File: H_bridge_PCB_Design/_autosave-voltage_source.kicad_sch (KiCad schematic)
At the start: 27 parts, among them IC1 LM2671M-3.3_NOPB, IC2 L7812ABD2T-TR, J15 TSW-102-15-T-S, U6 LD1086DT50TR, U8 3544-2

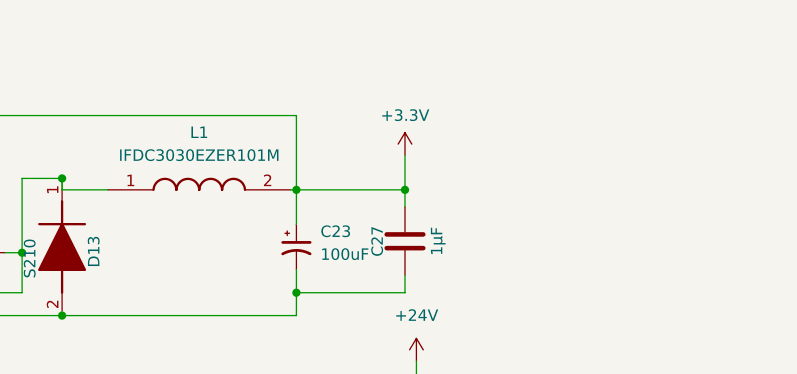
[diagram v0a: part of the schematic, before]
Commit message: -Changed PCB Layout now with 2x 3.3V also from usb, and to different ground planes -Measurement output now correctly parametrized -Stop sequence changed for SC protection
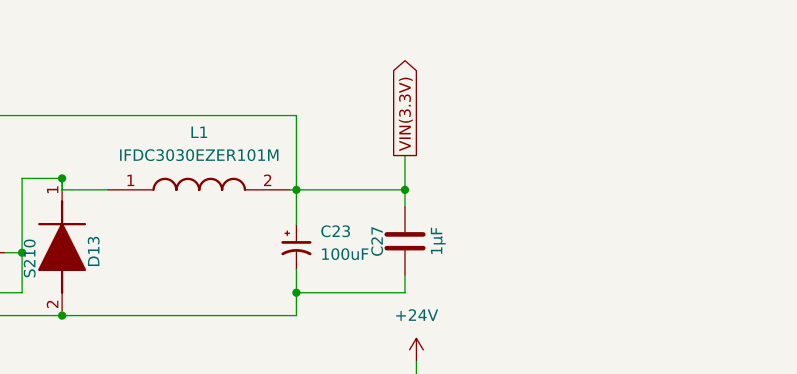
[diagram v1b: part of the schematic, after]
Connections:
- net +3.3V: no longer C23.1, C27.1, IC1.4 (FB), L1.2
- new net VIN(3.3V): C23.1, C27.1, IC1.4 (FB), L1.2
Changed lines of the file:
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@@
+		)
+	)
+	(global_label "VIN(3.3V)"
+		(shape output)
+		(at 220.98 35.56 90)
+		(fields_autoplaced yes)
+		(effects
+			(font
+				(size 1.27 1.27)
+			)
+			(justify left)
+		)
+		(property "Intersheetrefs" "${INTERSHEET_REFS}"
+			(at 220.98 23.7451 90)
+			(effects
+				(font
+					(size 1.27 1.27)
+				)
+				(justify left)
+				(hide yes)
+			)
 		)
 	)
@@
 			)
 		)
-	)
-	(symbol
-		(lib_id "power:+3.3V")
-		(at 220.98 35.56 0)
-		(unit 1)
-		(exclude_from_sim no)
-		(in_bom yes)
-		(on_board yes)
-		(dnp no)
-		(fields_autoplaced yes)
-		(property "Reference" "#PWR035"
-			(at 220.98 39.37 0)
-			(effects
-				(font
-					(size 1.27 1.27)
-				)
-				(hide yes)
-			)
-		)
-		(property "Value" "+3.3V"
-			(at 220.98 31.115 0)
-			(effects
-				(font
-					(size 1.27 1.27)
-				)
-			)
-		)
-		(property "Footprint" ""
-			(at 220.98 35.56 0)
-			(effects
-				(font
-					(size 1.27 1.27)
-				)
-				(hide yes)
-			)
-		)
-		(property "Datasheet" ""
-			(at 220.98 35.56 0)
-			(effects
-				(font
-					(size 1.27 1.27)
-				)
-				(hide yes)
-			)
-		)
-		(property "Description" "Power symbol creates a global label with name \"+3.3V\""
-			(at 220.98 35.56 0)
-			(effects
-				(font
-					(size 1.27 1.27)
-				)
-				(hide yes)
-			)
-		)
-		(pin "1"
-		)
-		(instances
-			(project ""
-				(path "/39329e70-3d95-44e7-ab4e-2263b2a8fd19/5cd83469-f4dc-4d9b-8949-703722184d70"
-					(reference "#PWR035")
-					(unit 1)
-				)
-			)
-		)
